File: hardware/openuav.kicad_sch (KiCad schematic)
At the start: 95 parts, among them J1 Conn_01x01, J10 Conn_01x01, J11 Conn_01x01, J12 Conn_01x01, J13 Conn_01x01, J14 Conn_01x01, J15 Conn_01x01, J16 Conn_01x01, J17 Conn_01x01, J18 Conn_01x01, J19 Conn_01x01, J2 Conn_01x01, J20 Conn_01x01, J21 Conn_01x01, J22 Conn_01x01, J23 Conn_01x01, J24 Conn_01x01, J25 Conn_01x01, J3 Conn_01x01, J4 Conn_01x01, J5 Conn_01x01, J6 Conn_01x01, J7 Conn_01x01, J8 Conn_01x01, J9 Conn_01x01, J99 USB_C_Receptacle_USB2.0, SW1 SW_Push, U1 STM32G431CBUx, U2 LPS22HH, U3 LSM6DSR, U6 W25N01GVZEIG, U7 TLV75733PDBV, U8 TLV75733PDBV

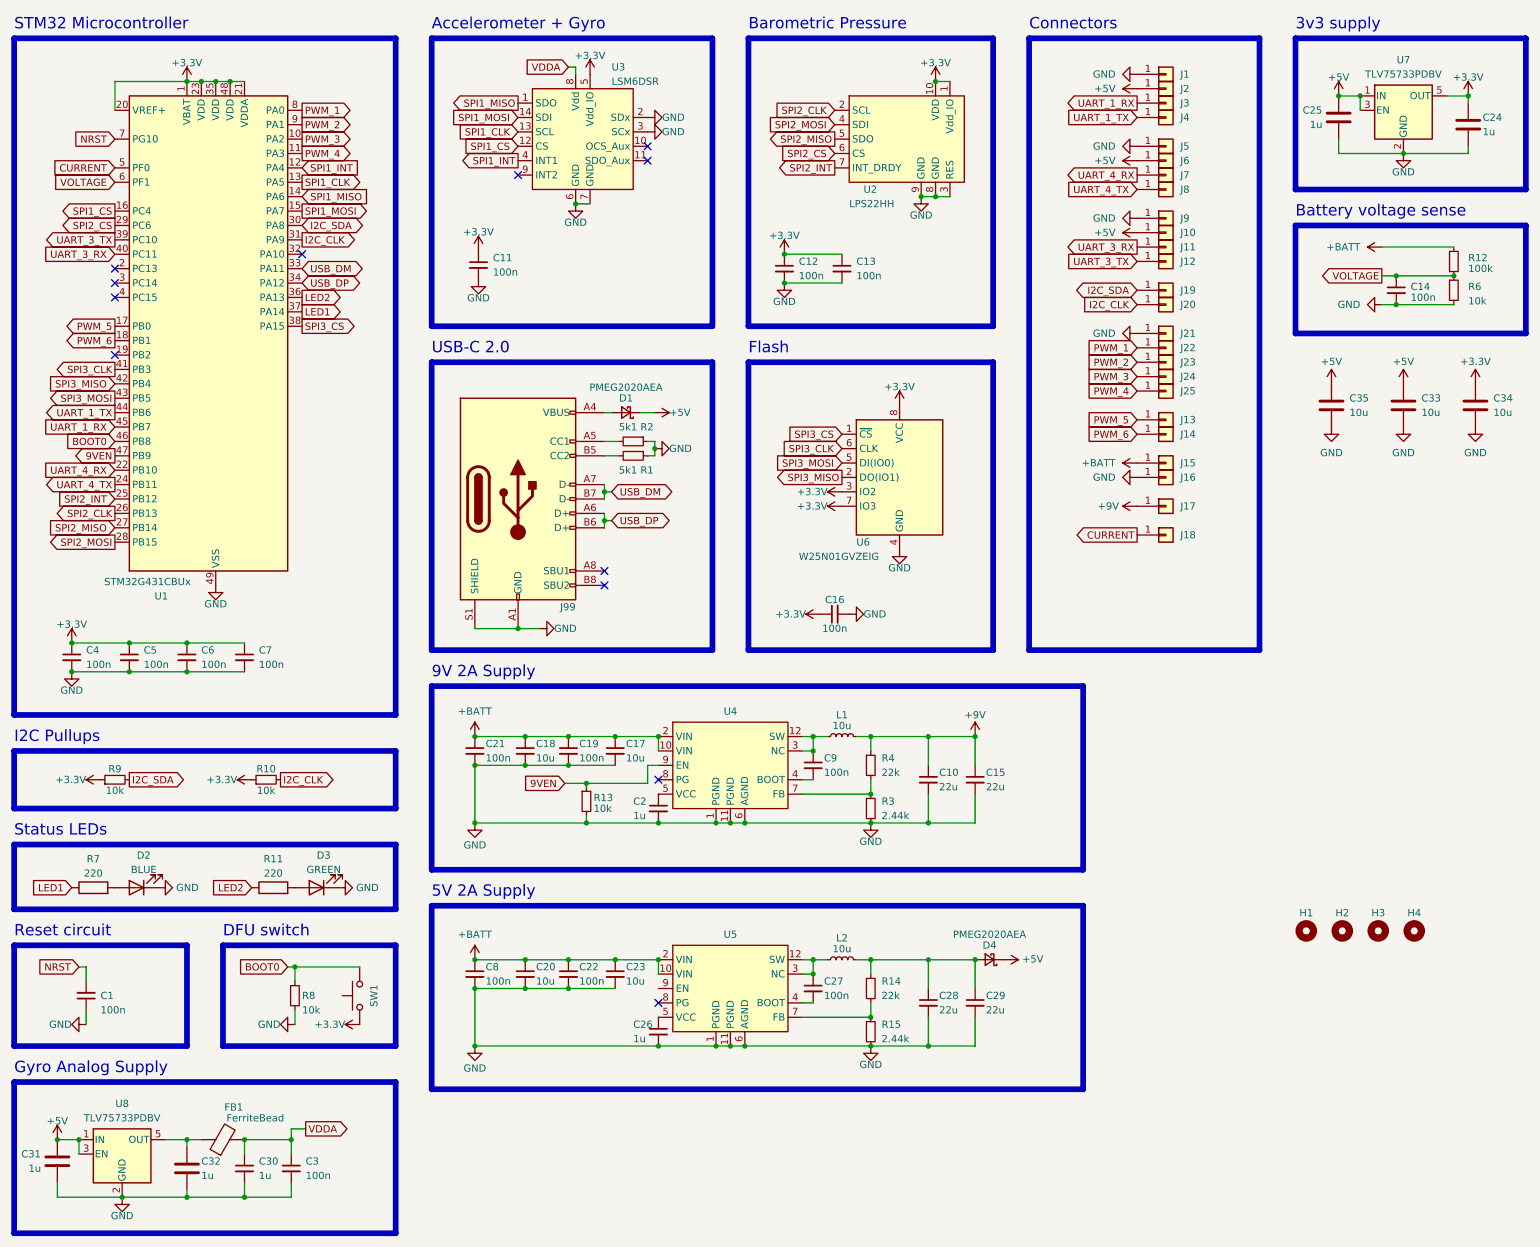
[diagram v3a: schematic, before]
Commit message: Revert v1 hardware, remove unused code for v2 hardware
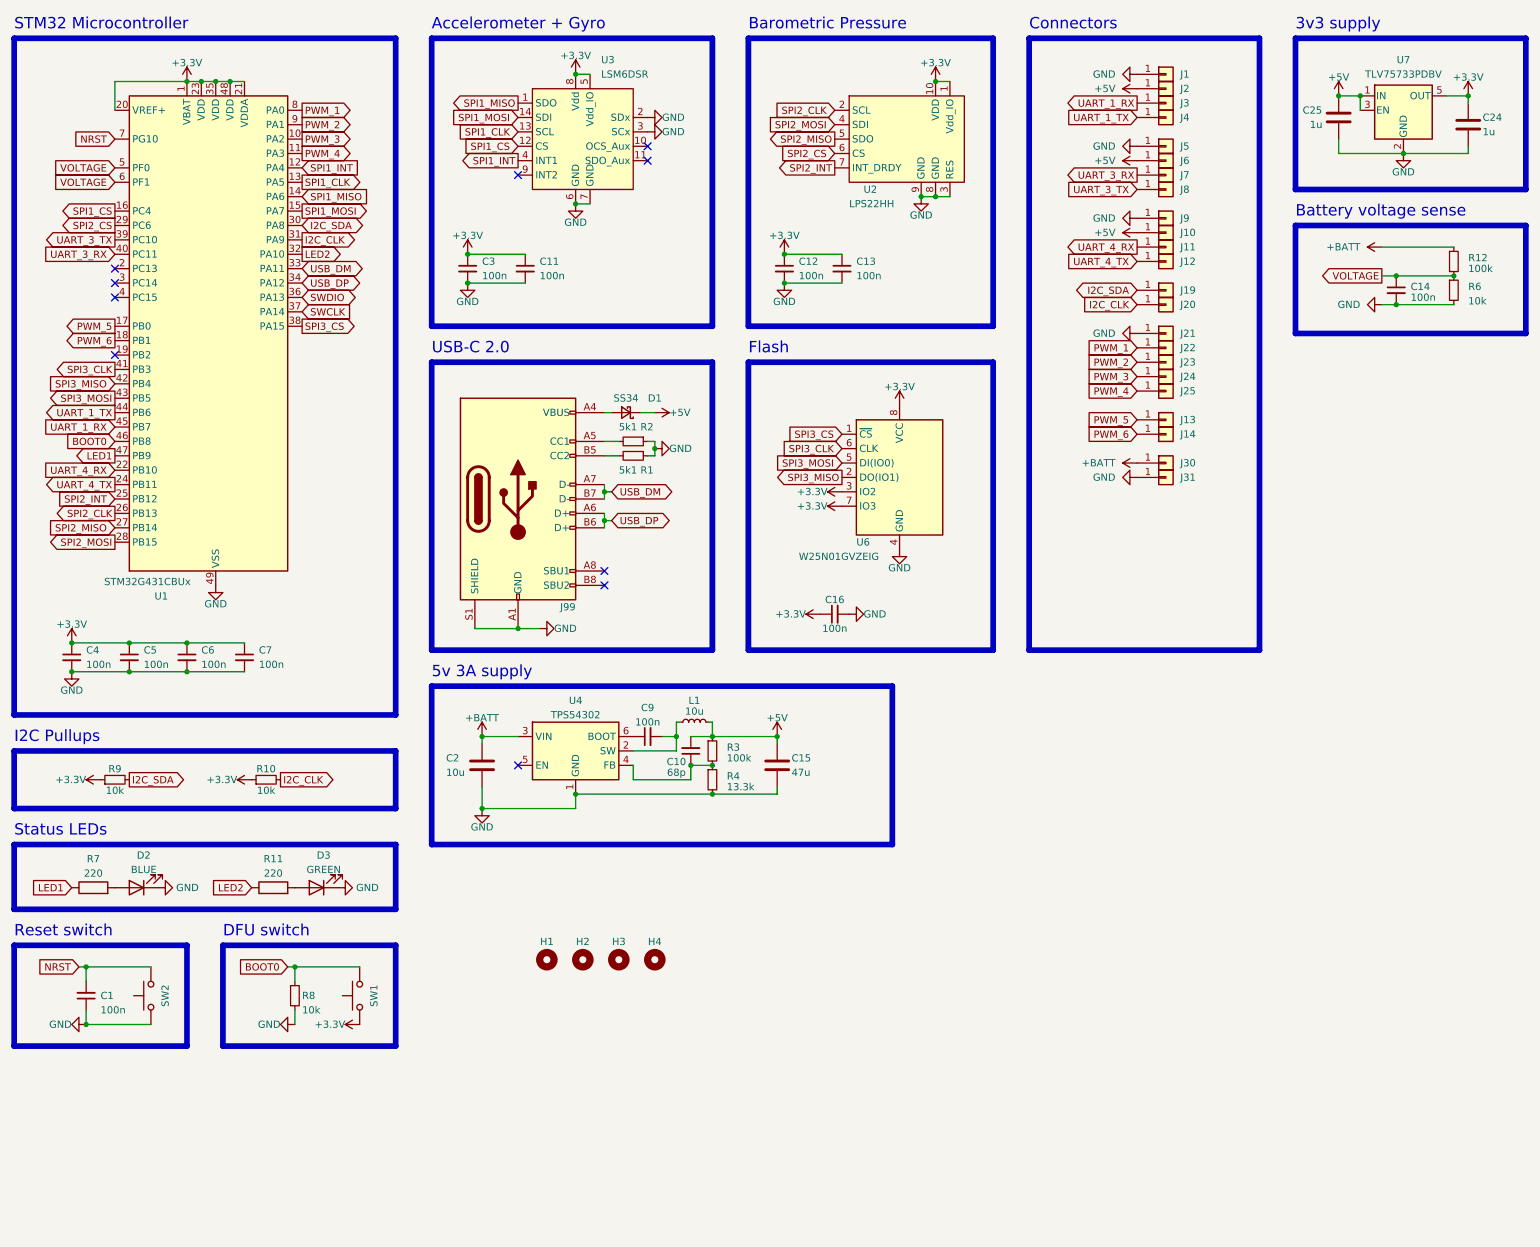
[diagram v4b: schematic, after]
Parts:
- removed C15, C28, C29: 22u, Capacitor_SMD:C_1206_3216Metric, symbol Device:C_Small
- removed C17, C18, C20, C23: 10u, Capacitor_SMD:C_1206_3216Metric, symbol Device:C_Small
- removed C19, C21, C22, C27, C8: 100n, Capacitor_SMD:C_0402_1005Metric, symbol Device:C_Small
- removed C2, C26, C30: 1u, Capacitor_SMD:C_0402_1005Metric, symbol Device:C_Small
- removed C31, C32: 1u, Capacitor_SMD:C_0402_1005Metric, symbol Device:C
- removed C33, C34, C35: 10u, Capacitor_SMD:C_0603_1608Metric, symbol Device:C
- removed D4: PMEG2020AEA, Diode_SMD:D_SOD-323, symbol Device:D_Schottky_Small
- removed FB1: FerriteBead, Inductor_SMD:L_0805_2012Metric, symbol Device:FerriteBead
- removed J15, J16: Conn_01x01, footprints:largepad, symbol Connector_Generic:Conn_01x01
- removed J17, J18: Conn_01x01, footprints:smallpad, symbol Connector_Generic:Conn_01x01
- removed L2: 10u, Inductor_SMD:L_Sunlord_MWSA0503S, symbol Device:L_Small
- removed R13: 10k, Resistor_SMD:R_0402_1005Metric, symbol Device:R_Small
- removed R14: 22k, Resistor_SMD:R_0402_1005Metric, symbol Device:R_Small
- removed R15: 2.44k, Resistor_SMD:R_0402_1005Metric, symbol Device:R_Small
- removed U4, U5: ~, footprints:RNX0012B, symbol openuav:LMR33630BRNXR
- removed U8: TLV75733PDBV, Package_TO_SOT_SMD:SOT-23-5, symbol Regulator_Linear:TLV75733PDBV
- added C15: 47u, Capacitor_SMD:C_1210_3225Metric, symbol Device:C
- added C2: 10u, Capacitor_SMD:C_1206_3216Metric, symbol Device:C
- added J30, J31: Conn_01x01, footprints:largepad, symbol Connector_Generic:Conn_01x01
- added SW2: SW_Push, Button_Switch_SMD:SW_SPST_B3U-1000P, symbol Switch:SW_Push
- added U4: TPS54302, Package_TO_SOT_SMD:SOT-23-6, symbol Regulator_Switching:TPS54302
- C10: value 22u -> 68p; footprint Capacitor_SMD:C_1206_3216Metric -> Capacitor_SMD:C_0402_1005Metric; LCSC C12891 -> C14441
- D1: value PMEG2020AEA -> SS34; footprint Diode_SMD:D_SOD-323 -> Diode_SMD:D_SMA; LCSC C389354 -> C8678
- L1: LCSC (none) -> C408412
- R3: value 2.44k -> 100k; LCSC (none) -> C25741
- R4: value 22k -> 13.3k; LCSC (none) -> C274352
- U3: LCSC C784817 -> C2655100
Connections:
- net 9VEN is gone; now on net LED1: U1.47 (PB9)
- net CURRENT is gone; now on net VOLTAGE: U1.5 (PF0)
- net VDDA is gone; now on net +3V3: C3.1, U3.8 (Vdd)
- net +5V: now also C10.2, L1.2, R3.1, C15.1
- net +BATT: now also C2.1, J30.1 (Pin_1), U4.3 (VIN)
- net GND: now also R4.2, C15.2, C2.2, J31.1 (Pin_1), SW2.1, U4.1 (GND); no longer C10.2, R3.2
- net LED1: no longer U1.37 (PA14)
- net LED2: now also U1.32 (PA10); no longer U1.36 (PA13)
- net NRST: now also SW2.2
- net UART_3_RX: now also J7.1 (Pin_1); no longer J11.1 (Pin_1)
- net UART_3_TX: now also J8.1 (Pin_1); no longer J12.1 (Pin_1)
- net UART_4_RX: now also J11.1 (Pin_1); no longer J7.1 (Pin_1)
- net UART_4_TX: now also J12.1 (Pin_1); no longer J8.1 (Pin_1)
- net at L1.1: now also C9.2, U4.2 (SW); no longer C9.1
- net +9V: no longer names the net of C10.1, R4.1
- net +9V: now also R3.2, U4.4 (FB); no longer L1.2
- new net: C9.1, U4.6 (BOOT)
- new net SWCLK: U1.37 (PA14)
- new net SWDIO: U1.36 (PA13)
- no-connect marks 12 -> 10
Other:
- note added: "5v 3A supply"
- note added: "Reset switch"
- note removed: "5V 2A Supply"
- note removed: "9V 2A Supply"
- note removed: "Gyro Analog Supply"
- note removed: "Reset circuit"
- moved on the sheet: C11, C3, H1, H2, H3, H4

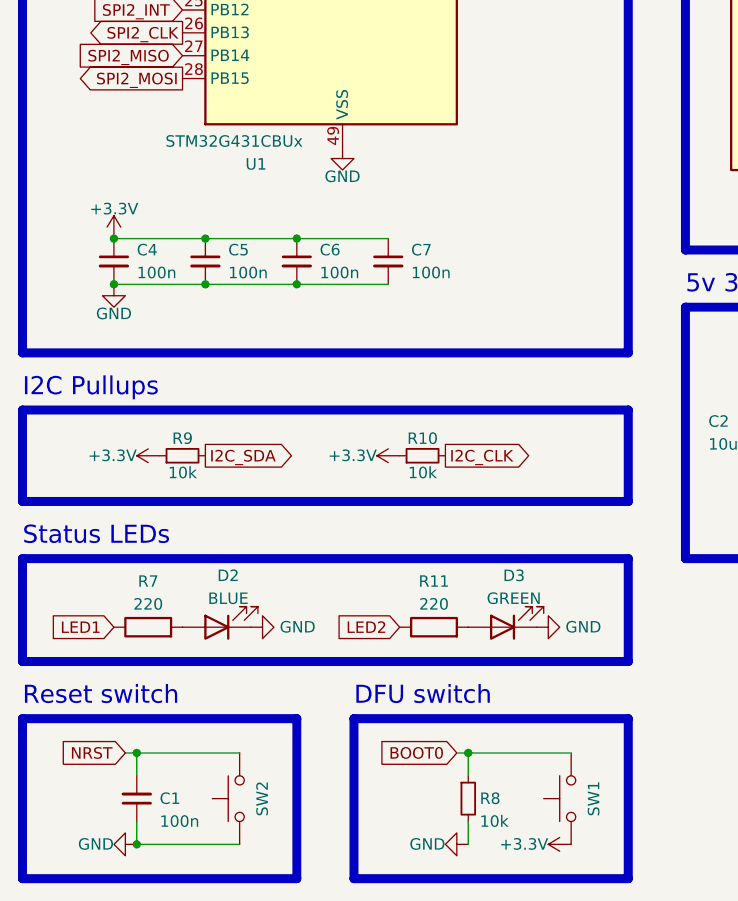
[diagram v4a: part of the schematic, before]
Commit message: Remove reset button
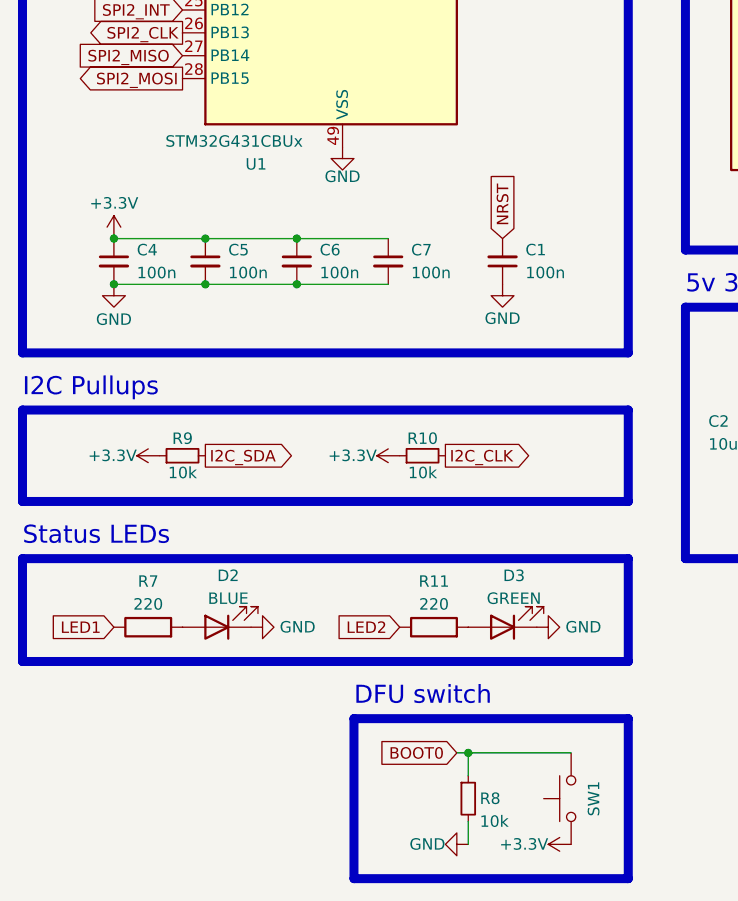
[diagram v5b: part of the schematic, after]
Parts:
- removed SW2: SW_Push, Button_Switch_SMD:SW_SPST_B3U-1000P, symbol Switch:SW_Push
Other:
- note removed: "Reset switch"
- moved on the sheet: C1
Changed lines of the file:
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@@
   (junction (at 114.3 151.13) (diameter 0) (color 0 0 0 0)
   )
-  (junction (at 27.94 191.77) (diameter 0) (color 0 0 0 0)
-  )
   (junction (at 50.8 25.4) (diameter 0) (color 0 0 0 0)
   )
@@
   (junction (at 45.72 129.54) (diameter 0) (color 0 0 0 0)
   )
-  (junction (at 27.94 181.61) (diameter 0) (color 0 0 0 0)
-  )
   (junction (at 48.26 25.4) (diameter 0) (color 0 0 0 0)
   )
@@
     (stroke (width 0) (type default))
   )
-  (wire (pts (xy 27.94 191.77) (xy 39.37 191.77))
-    (stroke (width 0) (type default))
-  )
   (wire (pts (xy 95.25 55.88) (xy 105.41 55.88))
     (stroke (width 0) (type default))
@@
     (stroke (width 0) (type default))
   )
-  (wire (pts (xy 27.94 181.61) (xy 39.37 181.61))
-    (stroke (width 0) (type default))
-  )
-  (wire (pts (xy 27.94 189.23) (xy 27.94 191.77))
-    (stroke (width 0) (type default))
-  )
   (wire (pts (xy 149.86 140.97) (xy 149.86 142.24))
     (stroke (width 0) (type default))
@@
     (stroke (width 0) (type default))
   )
-  (wire (pts (xy 27.94 181.61) (xy 27.94 184.15))
-    (stroke (width 0) (type default))
-  )
   (wire (pts (xy 256.54 64.77) (xy 259.08 64.77))
     (stroke (width 0) (type default))
@@
     (stroke (width 0) (type default))
   )
-  (wire (pts (xy 26.67 181.61) (xy 27.94 181.61))
-    (stroke (width 0) (type default))
-  )
   (wire (pts (xy 271.78 38.1) (xy 271.78 36.83))
     (stroke (width 0) (type default))
@@
     (fill (type none))
   )
-  (rectangle (start 15.24 177.8) (end 45.72 195.58)
-    (stroke (width 1) (type default))
-    (fill (type none))
-  )
   (rectangle (start 15.24 17.78) (end 82.55 137.16)
     (stroke (width 1) (type default))
@@
     (effects (font (size 2 2)) (justify left bottom))
   )
-  (text "Reset switch" (at 15.24 176.53 0)
-    (effects (font (size 2 2)) (justify left bottom))
-  )
   (text "DFU switch" (at 52.07 176.53 0)
     (effects (font (size 2 2)) (justify left bottom))
@@
     )
   )
-  (global_label "NRST" (shape input) (at 26.67 181.61 180) (fields_autoplaced)
-    (effects (font (size 1.27 1.27)) (justify right))
-    (property "Intersheetrefs" "${INTERSHEET_REFS}" (at 19.4793 181.5306 0)
-      (effects (font (size 1.27 1.27)) (justify right) hide)
+  (global_label "NRST" (shape input) (at 68.58 124.46 90) (fields_autoplaced)
+    (effects (font (size 1.27 1.27)) (justify left))
+    (property "Intersheetrefs" "${INTERSHEET_REFS}" (at 68.58 116.6972 90)
+      (effects (font (size 1.27 1.27)) (justify left) hide)
     )
   )
@@
     )
   )
-  (symbol (lib_id "power:GND") (at 27.94 191.77 270) (unit 1)
+  (symbol (lib_id "power:GND") (at 68.58 129.54 0) (unit 1)
     (in_bom yes) (on_board yes) (dnp no)
-    (property "Reference" "#PWR047" (at 21.59 191.77 0)
+    (property "Reference" "#PWR047" (at 68.58 135.89 0)
       (effects (font (size 1.27 1.27)) hide)
     )
-    (property "Value" "GND" (at 25.4 191.77 90)
-      (effects (font (size 1.27 1.27)) (justify right))
+    (property "Value" "GND" (at 68.58 133.35 0)
+      (effects (font (size 1.27 1.27)))
     )
-    (property "Footprint" "" (at 27.94 191.77 0)
+    (property "Footprint" "" (at 68.58 129.54 0)
       (effects (font (size 1.27 1.27)) hide)
     )
-    (property "Datasheet" "" (at 27.94 191.77 0)
+    (property "Datasheet" "" (at 68.58 129.54 0)
       (effects (font (size 1.27 1.27)) hide)
     )
@@
     )
   )
-  (symbol (lib_id "Switch:SW_Push") (at 39.37 186.69 90) (unit 1)
-    (in_bom yes) (on_board yes) (dnp no)
-    (property "Reference" "SW2" (at 41.91 186.69 0)
-      (effects (font (size 1.27 1.27)))
-    )
-    (property "Value" "SW_Push" (at 41.91 186.69 0)
-      (effects (font (size 1.27 1.27)) hide)
-    )
-    (property "Footprint" "Button_Switch_SMD:SW_SPST_B3U-1000P" (at 34.29 186.69 0)
-      (effects (font (size 1.27 1.27)) hide)
-    )
-    (property "Datasheet" "~" (at 34.29 186.69 0)
-      (effects (font (size 1.27 1.27)) hide)
-    )
-    (property "LCSC" "C231329" (at 39.37 186.69 0)
-      (effects (font (size 1.27 1.27)) hide)
-    )
-    (pin "1")
-    (pin "2")
-    (instances
-      (project "openuav"
-        (path "/e63e39d7-6ac0-4ffd-8aa3-1841a4541b55"
-          (reference "SW2") (unit 1)
-        )
-      )
-    )
-  )
   (symbol (lib_id "Device:C_Small") (at 151.13 58.42 0) (unit 1)
     (in_bom yes) (on_board yes) (dnp no) (fields_autoplaced)
@@
       (effects (font (size 1.27 1.27)) hide)
     )
-    (property "Value" "GND" (at 25.4 132.08 0)
+    (property "Value" "GND" (at 25.4 132.715 0)
       (effects (font (size 1.27 1.27)) (justify top))
     )
@@
     )
   )
-  (symbol (lib_id "Device:C_Small") (at 27.94 186.69 180) (unit 1)
+  (symbol (lib_id "Device:C_Small") (at 68.58 127 180) (unit 1)
     (in_bom yes) (on_board yes) (dnp no)
-    (property "Reference" "C1" (at 30.48 186.69 0)
+    (property "Reference" "C1" (at 71.12 125.73 0)
       (effects (font (size 1.27 1.27)) (justify right))
     )
-    (property "Value" "100n" (at 30.48 189.23 0)
+    (property "Value" "100n" (at 71.12 128.27 0)
       (effects (font (size 1.27 1.27)) (justify right))
     )
-    (property "Footprint" "Capacitor_SMD:C_0402_1005Metric" (at 27.94 186.69 0)
+    (property "Footprint" "Capacitor_SMD:C_0402_1005Metric" (at 68.58 127 0)
       (effects (font (size 1.27 1.27)) hide)
     )
-    (property "Datasheet" "~" (at 27.94 186.69 0)
+    (property "Datasheet" "~" (at 68.58 127 0)
       (effects (font (size 1.27 1.27)) hide)
     )
-    (property "LCSC" "C1525" (at 27.94 186.69 0)
+    (property "LCSC" "C1525" (at 68.58 127 0)
       (effects (font (size 1.27 1.27)) hide)
     )
@@
       (effects (font (size 1.27 1.27)) hide)
     )
-    (property "Value" "+3.3V" (at 25.4 121.92 0)
+    (property "Value" "+3.3V" (at 25.4 121.285 0)
       (effects (font (size 1.27 1.27)) (justify bottom))
     )

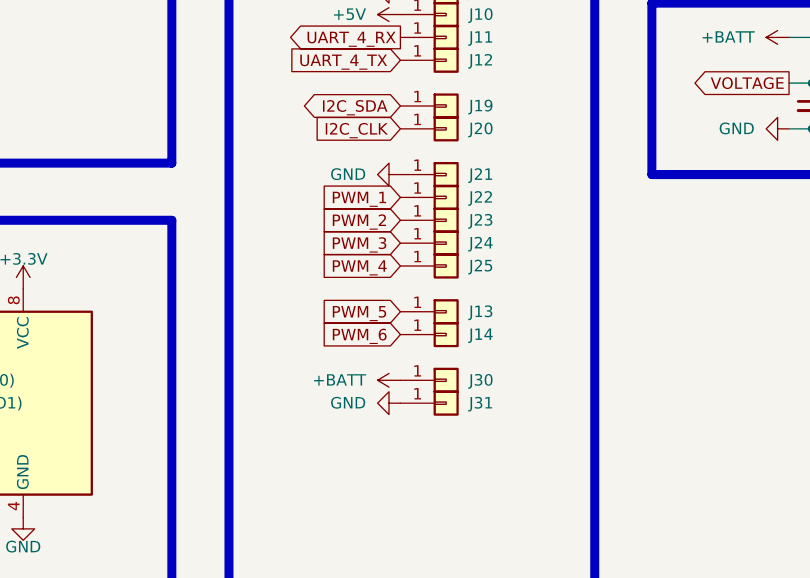
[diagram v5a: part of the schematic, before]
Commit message: Move DFU button
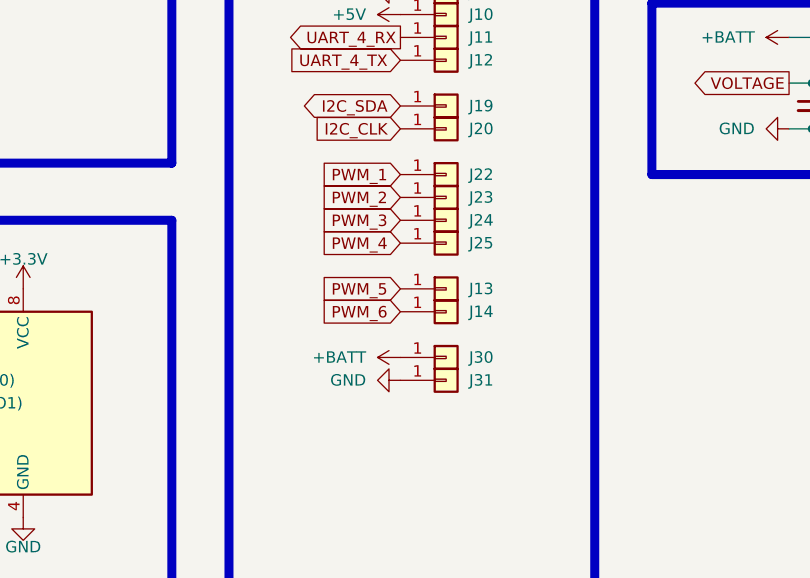
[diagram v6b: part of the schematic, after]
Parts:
- removed J21: Conn_01x01, footprints:smallpad, symbol Connector_Generic:Conn_01x01
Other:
- moved on the sheet: J13, J14, J22, J23, J24, J25, J30, J31
